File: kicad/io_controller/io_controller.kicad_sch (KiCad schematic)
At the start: 20 parts

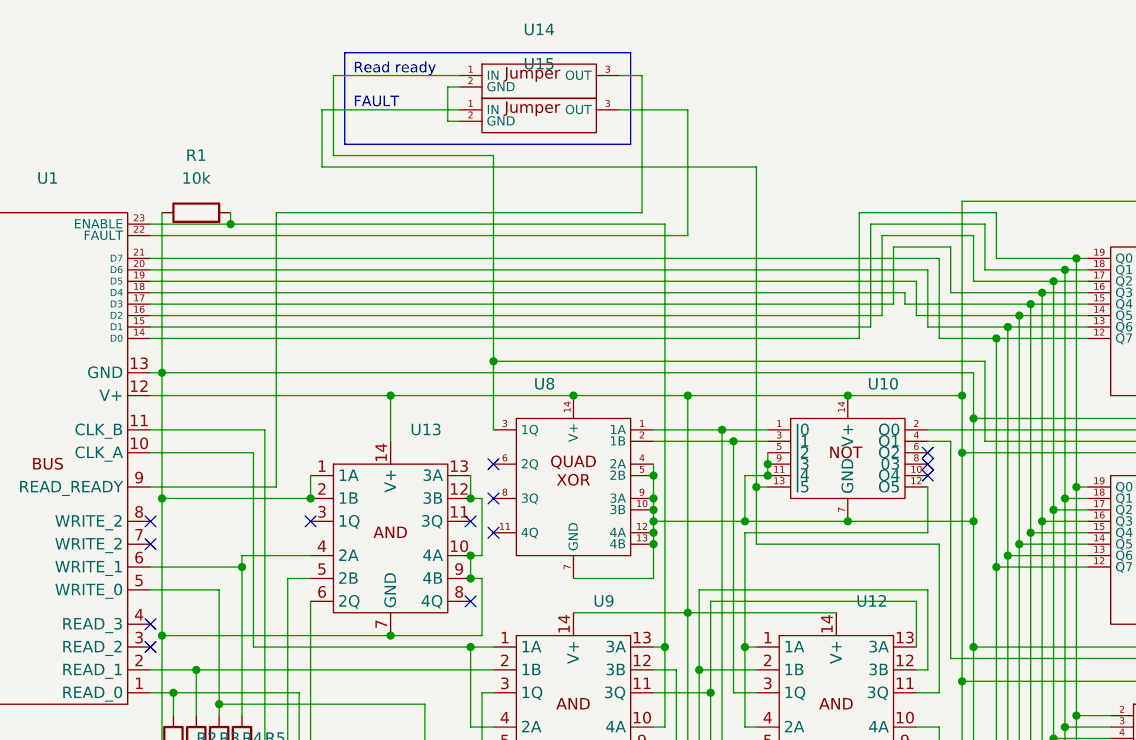
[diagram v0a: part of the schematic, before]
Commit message: Working on GPRAM schematic
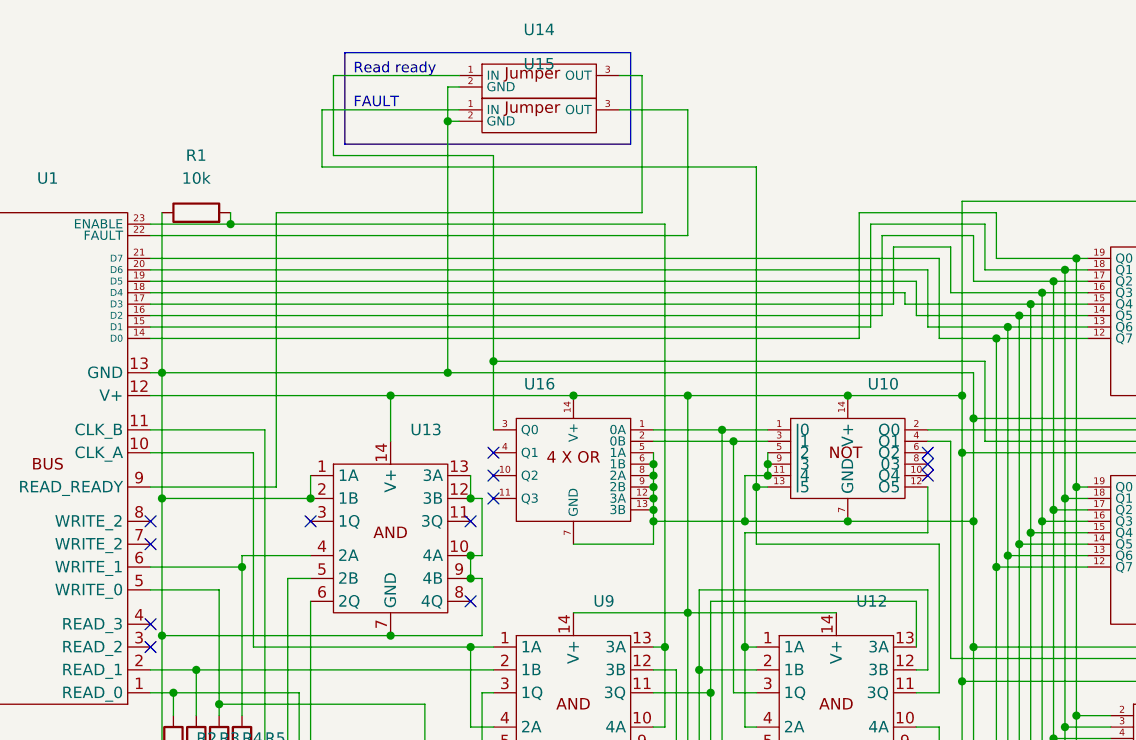
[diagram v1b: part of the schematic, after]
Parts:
- removed U8: ~, Package_DIP:DIP-14_W7.62mm, symbol custom_symbol_lib:4x_XOR
- added U16: ~, Package_DIP:DIP-14_W7.62mm, symbol custom_symbol_lib:quad_OR
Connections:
- net at R1.1, R2.2, R3.2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: now also U14.2 (GND), U15.2 (GND), U16.12 (3A), U16.13 (3B), U16.5 (1A), U16.6 (1B), U16.7 (GND), U16.8 (2A), U16.9 (2B)
- net at U14.1 (IN), U2.11 (CLK), U6.11 (CLK): now also U16.3 (Q0)
- net at U1.12 (V+), U10.14 (V+), U11.14 (V+)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: now also U16.14 (V+)
- net at U10.1 (I0), U12.6 (2Q): now also U16.1 (0A)
- net at U10.3 (I1), U12.3 (1Q): now also U16.2 (0B)
